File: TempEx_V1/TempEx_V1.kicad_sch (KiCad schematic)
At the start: 1 part, among them J2 Conn_01x10

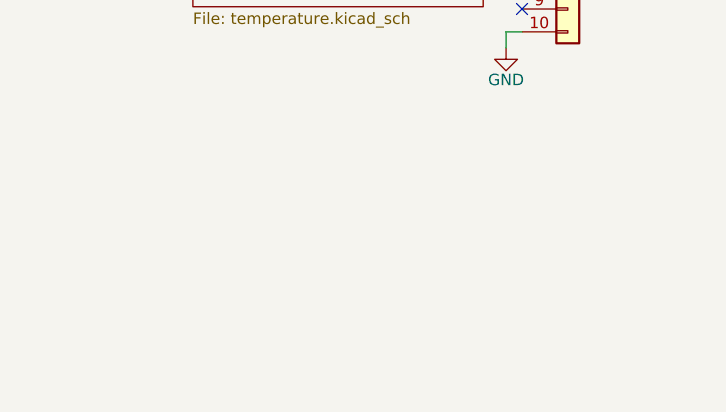
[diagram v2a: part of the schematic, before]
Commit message: Stitching missing
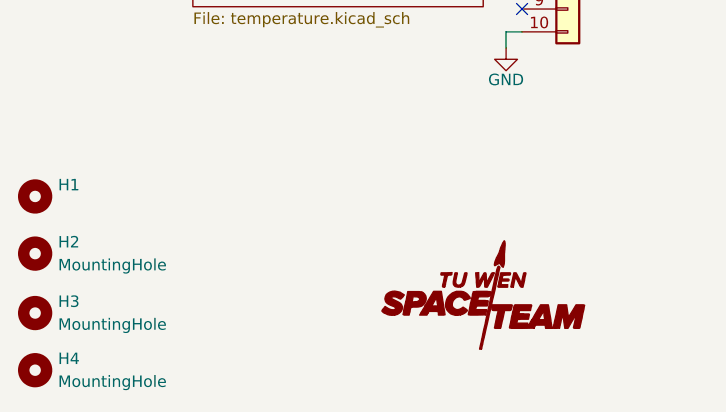
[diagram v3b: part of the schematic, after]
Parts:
- added H1: (no value), symbol Mechanical:MountingHole
- added H2, H3, H4: MountingHole, symbol Mechanical:MountingHole
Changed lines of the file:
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@@
     (stroke (width 0) (type default) (color 0 0 0 0))
+  )
+  (symbol (lib_id "TXV_Library_Symbols:SpaceTeam_LOGO") (at 194.564 104.648 0) (unit 1)
+    (in_bom yes) (on_board yes) (fields_autoplaced)
+    (property "Reference" "#G1" (id 0) (at 194.564 109.8804 0)
+      (effects (font (size 1.524 1.524)) hide)
+    )
+    (property "Value" "" (id 1) (at 194.564 99.4156 0)
+      (effects (font (size 1.524 1.524)) hide)
+    )
+    (property "Footprint" "" (id 2) (at 194.564 104.648 0)
+      (effects (font (size 1.27 1.27)) hide)
+    )
+    (property "Datasheet" "" (id 3) (at 194.564 104.648 0)
+      (effects (font (size 1.27 1.27)) hide)
+    )
+  )
+  (symbol (lib_id "Mechanical:MountingHole") (at 144.78 93.726 0) (unit 1)
+    (in_bom yes) (on_board yes) (fields_autoplaced)
+    (property "Reference" "H1" (id 0) (at 147.32 92.4559 0)
+      (effects (font (size 1.27 1.27)) (justify left))
+    )
+    (property "Value" "" (id 1) (at 147.32 94.9959 0)
+      (effects (font (size 1.27 1.27)) (justify left))
+    )
+    (property "Footprint" "" (id 2) (at 144.78 93.726 0)
+      (effects (font (size 1.27 1.27)) hide)
+    )
+    (property "Datasheet" "~" (id 3) (at 144.78 93.726 0)
+      (effects (font (size 1.27 1.27)) hide)
+    )
+  )
+  (symbol (lib_id "Mechanical:MountingHole") (at 144.78 113.03 0) (unit 1)
+    (in_bom yes) (on_board yes) (fields_autoplaced)
+    (property "Reference" "H4" (id 0) (at 147.32 111.7599 0)
+      (effects (font (size 1.27 1.27)) (justify left))
+    )
+    (property "Value" "MountingHole" (id 1) (at 147.32 114.2999 0)
+      (effects (font (size 1.27 1.27)) (justify left))
+    )
+    (property "Footprint" "" (id 2) (at 144.78 113.03 0)
+      (effects (font (size 1.27 1.27)) hide)
+    )
+    (property "Datasheet" "~" (id 3) (at 144.78 113.03 0)
+      (effects (font (size 1.27 1.27)) hide)
+    )
   )
   (symbol (lib_id "power:+3.3V") (at 197.358 49.784 0) (unit 1)
@@
     )
     (pin "1")
+  )
+  (symbol (lib_id "Mechanical:MountingHole") (at 144.78 100.076 0) (unit 1)
+    (in_bom yes) (on_board yes) (fields_autoplaced)
+    (property "Reference" "H2" (id 0) (at 147.32 98.8059 0)
+      (effects (font (size 1.27 1.27)) (justify left))
+    )
+    (property "Value" "MountingHole" (id 1) (at 147.32 101.3459 0)
+      (effects (font (size 1.27 1.27)) (justify left))
+    )
+    (property "Footprint" "" (id 2) (at 144.78 100.076 0)
+      (effects (font (size 1.27 1.27)) hide)
+    )
+    (property "Datasheet" "~" (id 3) (at 144.78 100.076 0)
+      (effects (font (size 1.27 1.27)) hide)
+    )
+  )
+  (symbol (lib_id "Mechanical:MountingHole") (at 144.78 106.68 0) (unit 1)
+    (in_bom yes) (on_board yes) (fields_autoplaced)
+    (property "Reference" "H3" (id 0) (at 147.32 105.4099 0)
+      (effects (font (size 1.27 1.27)) (justify left))
+    )
+    (property "Value" "MountingHole" (id 1) (at 147.32 107.9499 0)
+      (effects (font (size 1.27 1.27)) (justify left))
+    )
+    (property "Footprint" "" (id 2) (at 144.78 106.68 0)
+      (effects (font (size 1.27 1.27)) hide)
+    )
+    (property "Datasheet" "~" (id 3) (at 144.78 106.68 0)
+      (effects (font (size 1.27 1.27)) hide)
+    )
   )
   (symbol (lib_id "Connector_Generic:Conn_01x10") (at 203.962 62.738 0) (unit 1)
@@
       (reference "#FLG0104") (unit 1) (value "PWR_FLAG") (footprint "")
     )
+    (path "/0c338ea3-b07d-4404-9ec8-feface7d9dbf"
+      (reference "#G1") (unit 1) (value "SpaceTeam_LOGO") (footprint "TXV_Library_Footprints:ST_Logo_new")
+    )
     (path "/4d24f783-afb0-42a0-9683-e8b59325e024"
       (reference "#PWR01") (unit 1) (value "+3.3V") (footprint "")
@@
       (reference "#PWR03") (unit 1) (value "+3.3V") (footprint "")
     )
+    (path "/ff60da9d-fe92-4759-b91e-bcaff4d8cbf3/4527f044-2daf-485b-b819-36ca805762b3/d555a2dd-9f3d-4a17-afc2-dea0736c0972"
+      (reference "#PWR04") (unit 1) (value "GNDD") (footprint "")
+    )
     (path "/ff60da9d-fe92-4759-b91e-bcaff4d8cbf3/4527f044-2daf-485b-b819-36ca805762b3/cdf301ef-3964-478d-be2a-ef4a338584be"
       (reference "#PWR05") (unit 1) (value "GND") (footprint "")
@@
       (reference "#PWR029") (unit 1) (value "GND") (footprint "")
     )
+    (path "/ff60da9d-fe92-4759-b91e-bcaff4d8cbf3/4527f044-2daf-485b-b819-36ca805762b3/ea815632-2522-456c-9c06-1698b52e8f45"
+      (reference "#PWR030") (unit 1) (value "GND") (footprint "")
+    )
+    (path "/ff60da9d-fe92-4759-b91e-bcaff4d8cbf3/2fcadadb-cf12-48e1-bc94-79ddc336a35a/d555a2dd-9f3d-4a17-afc2-dea0736c0972"
+      (reference "#PWR031") (unit 1) (value "GNDD") (footprint "")
+    )
+    (path "/ff60da9d-fe92-4759-b91e-bcaff4d8cbf3/2fcadadb-cf12-48e1-bc94-79ddc336a35a/ea815632-2522-456c-9c06-1698b52e8f45"
+      (reference "#PWR032") (unit 1) (value "GND") (footprint "")
+    )
+    (path "/ff60da9d-fe92-4759-b91e-bcaff4d8cbf3/e33bfa0c-1610-4b4a-a9b3-53bc411573a1/d555a2dd-9f3d-4a17-afc2-dea0736c0972"
+      (reference "#PWR033") (unit 1) (value "GNDD") (footprint "")
+    )
+    (path "/ff60da9d-fe92-4759-b91e-bcaff4d8cbf3/e33bfa0c-1610-4b4a-a9b3-53bc411573a1/ea815632-2522-456c-9c06-1698b52e8f45"
+      (reference "#PWR034") (unit 1) (value "GND") (footprint "")
+    )
+    (path "/ff60da9d-fe92-4759-b91e-bcaff4d8cbf3/8f9eb8fb-a7e6-455c-b83f-2da0b27d6aa2/d555a2dd-9f3d-4a17-afc2-dea0736c0972"
+      (reference "#PWR035") (unit 1) (value "GNDD") (footprint "")
+    )
+    (path "/ff60da9d-fe92-4759-b91e-bcaff4d8cbf3/8f9eb8fb-a7e6-455c-b83f-2da0b27d6aa2/ea815632-2522-456c-9c06-1698b52e8f45"
+      (reference "#PWR036") (unit 1) (value "GND") (footprint "")
+    )
     (path "/f4d47dd2-1d26-4141-aaca-5b80d4b022a5"
       (reference "#PWR0101") (unit 1) (value "GND") (footprint "")
@@
       (reference "C12") (unit 1) (value "100n") (footprint "Capacitor_SMD:C_0603_1608Metric_Pad1.08x0.95mm_HandSolder")
     )
+    (path "/288e24d6-9b70-4fdb-b0a8-e9b4f4fb7ddd"
+      (reference "H1") (unit 1) (value "MountingHole") (footprint "MountingHole:MountingHole_2.1mm")
+    )
+    (path "/542ce7af-3ca5-4714-ae7c-6ac8ed77c999"
+      (reference "H2") (unit 1) (value "MountingHole") (footprint "MountingHole:MountingHole_2.1mm")
+    )
+    (path "/62573da8-02a2-4561-a2ba-49429c19f315"
+      (reference "H3") (unit 1) (value "MountingHole") (footprint "MountingHole:MountingHole_2.1mm")
+    )
+    (path "/341ebe66-fa98-4e52-9006-945bac32be9f"
+      (reference "H4") (unit 1) (value "MountingHole") (footprint "MountingHole:MountingHole_2.1mm")
+    )
     (path "/ff60da9d-fe92-4759-b91e-bcaff4d8cbf3/4527f044-2daf-485b-b819-36ca805762b3/e1a1d094-3f6d-4ef4-9264-398b3bf59383"
       (reference "J1") (unit 1) (value "Conn_01x02") (footprint "Connector_Molex:Molex_SL_171971-0002_1x02_P2.54mm_Vertical")
@@
       (reference "J5") (unit 1) (value "Conn_01x02") (footprint "Connector_Molex:Molex_SL_171971-0002_1x02_P2.54mm_Vertical")
     )
+    (path "/ff60da9d-fe92-4759-b91e-bcaff4d8cbf3/4527f044-2daf-485b-b819-36ca805762b3/5ebbba19-51ee-4b6c-aa31-68e14a7a0569"
+      (reference "NT1") (unit 1) (value "NetTie_2") (footprint "NetTie:NetTie-2_SMD_Pad0.5mm")
+    )
+    (path "/ff60da9d-fe92-4759-b91e-bcaff4d8cbf3/2fcadadb-cf12-48e1-bc94-79ddc336a35a/5ebbba19-51ee-4b6c-aa31-68e14a7a0569"
+      (reference "NT2") (unit 1) (value "NetTie_2") (footprint "NetTie:NetTie-2_SMD_Pad0.5mm")
+    )
+    (path "/ff60da9d-fe92-4759-b91e-bcaff4d8cbf3/e33bfa0c-1610-4b4a-a9b3-53bc411573a1/5ebbba19-51ee-4b6c-aa31-68e14a7a0569"
+      (reference "NT3") (unit 1) (value "NetTie_2") (footprint "NetTie:NetTie-2_SMD_Pad0.5mm")
+    )
+    (path "/ff60da9d-fe92-4759-b91e-bcaff4d8cbf3/8f9eb8fb-a7e6-455c-b83f-2da0b27d6aa2/5ebbba19-51ee-4b6c-aa31-68e14a7a0569"
+      (reference "NT4") (unit 1) (value "NetTie_2") (footprint "NetTie:NetTie-2_SMD_Pad0.5mm")
+    )
     (path "/ff60da9d-fe92-4759-b91e-bcaff4d8cbf3/4527f044-2daf-485b-b819-36ca805762b3/f10a054e-80b8-470b-928c-dc3212fd858d"

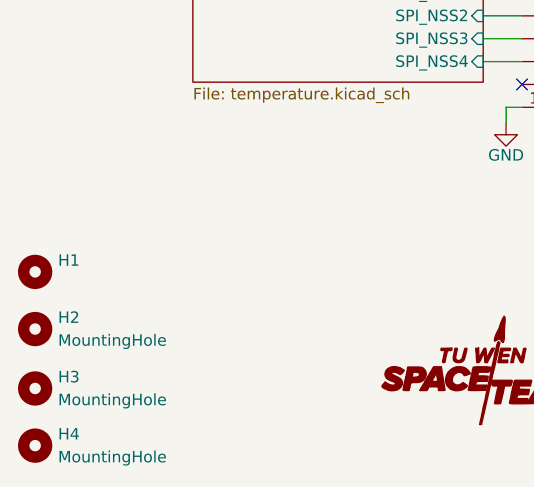
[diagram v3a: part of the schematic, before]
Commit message: Updated GND
All GNDD switched to GND
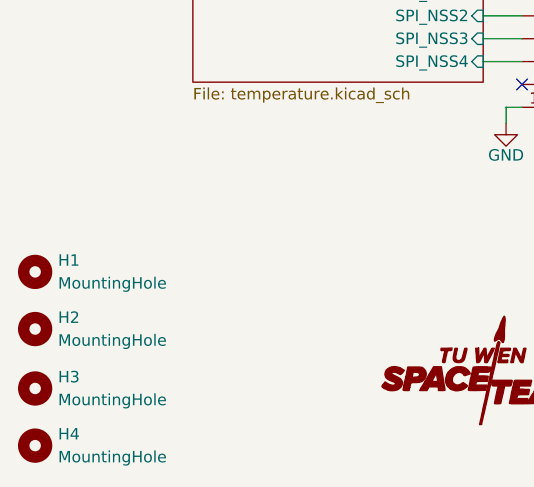
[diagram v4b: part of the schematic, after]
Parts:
- H1: value (none) -> MountingHole; footprint (none) -> MountingHole:MountingHole_2.1mm
- H2, H3, H4: footprint (none) -> MountingHole:MountingHole_2.1mm

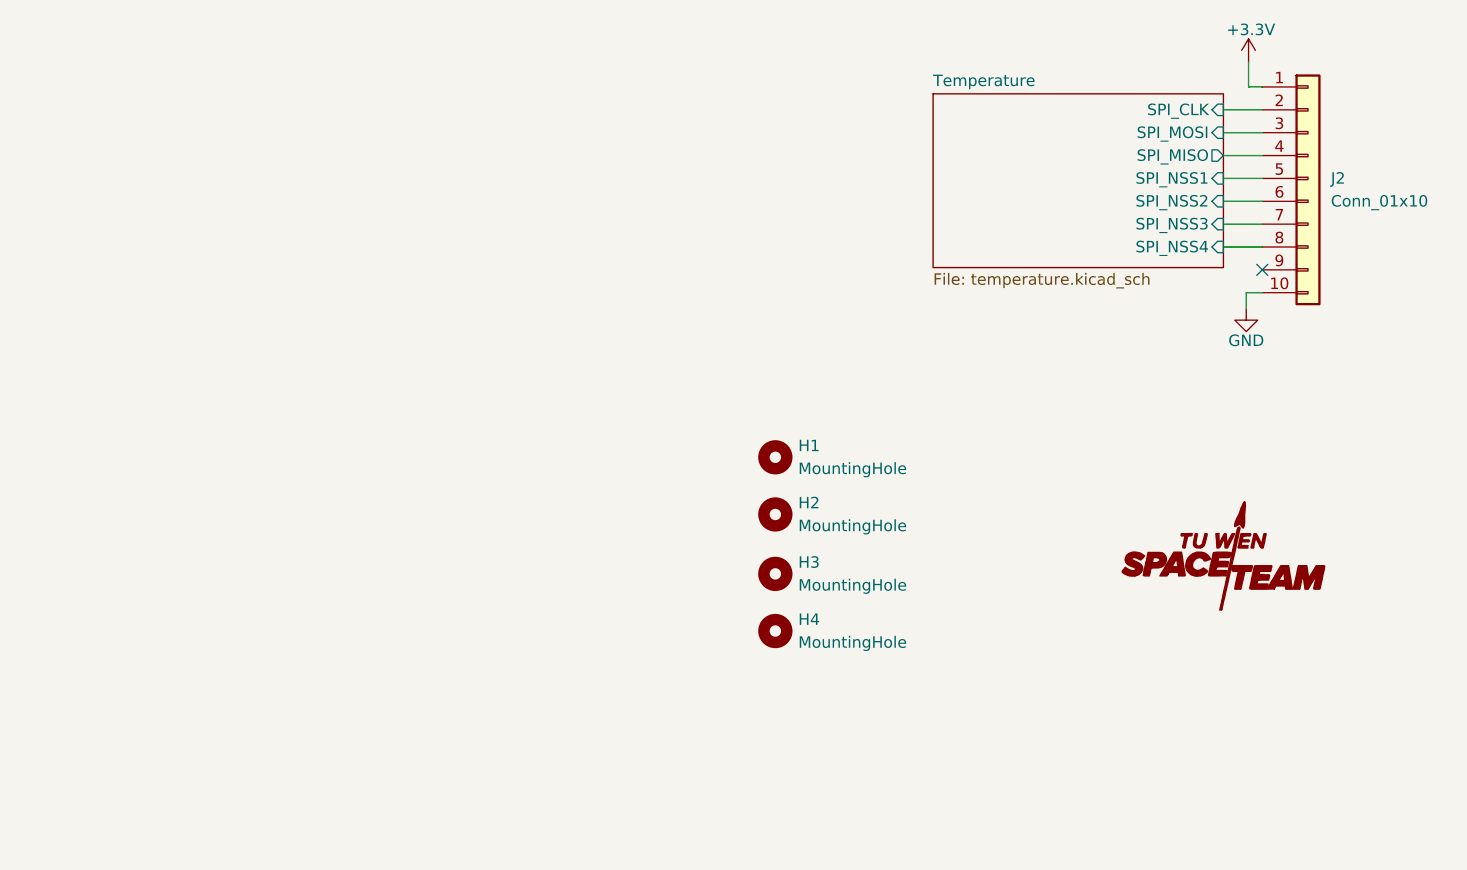
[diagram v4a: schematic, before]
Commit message: Layer change + 4 pin setup + stitching
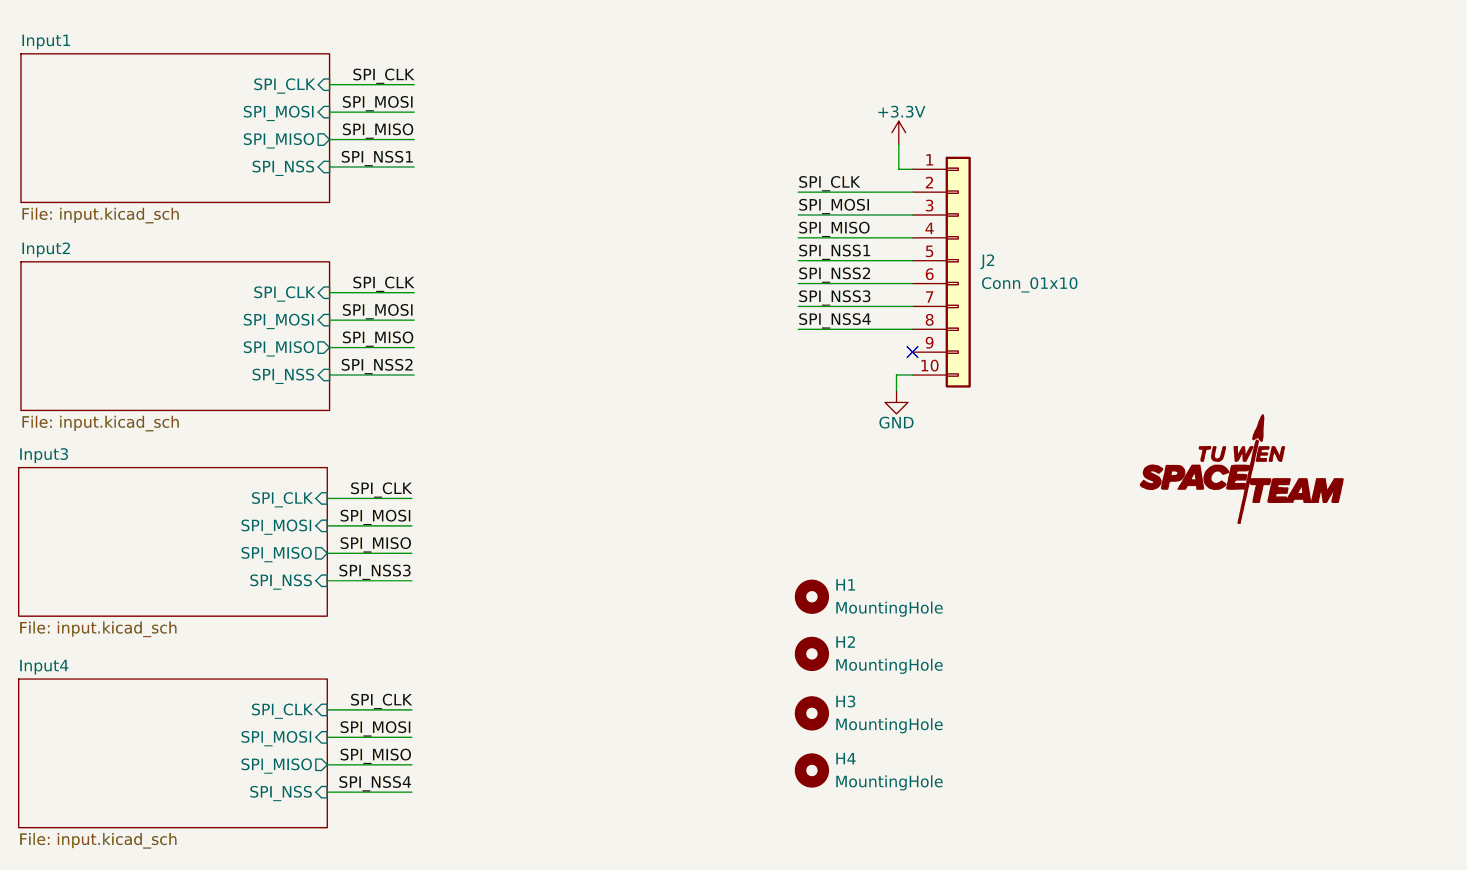
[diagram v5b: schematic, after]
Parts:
- added G1: SpaceTeam_LOGO, TXV_Library_Footprints:ST_Logo_new, symbol TXV_Library_Symbols:SpaceTeam_LOGO
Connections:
- net Temperature/SPI_CLK renamed SPI_CLK
- net Temperature/SPI_MISO renamed SPI_MISO
- net Temperature/SPI_MOSI renamed SPI_MOSI
- net Temperature/SPI_NSS1 renamed SPI_NSS1
- net Temperature/SPI_NSS2 renamed SPI_NSS2
- net Temperature/SPI_NSS3 renamed SPI_NSS3
- net Temperature/SPI_NSS4 renamed SPI_NSS4
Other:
- removed sheet Temperature
- added sheet Input1 (input.kicad_sch)
- added sheet Input2 (input.kicad_sch)
- added sheet Input3 (input.kicad_sch)
- added sheet Input4 (input.kicad_sch)
- moved on the sheet: H1, H2, H3, H4, J2
